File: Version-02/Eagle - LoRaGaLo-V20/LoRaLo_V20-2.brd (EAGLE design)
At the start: 69.5 x 82.5 mm, 31 parts, among them U2 RFM95WSMD

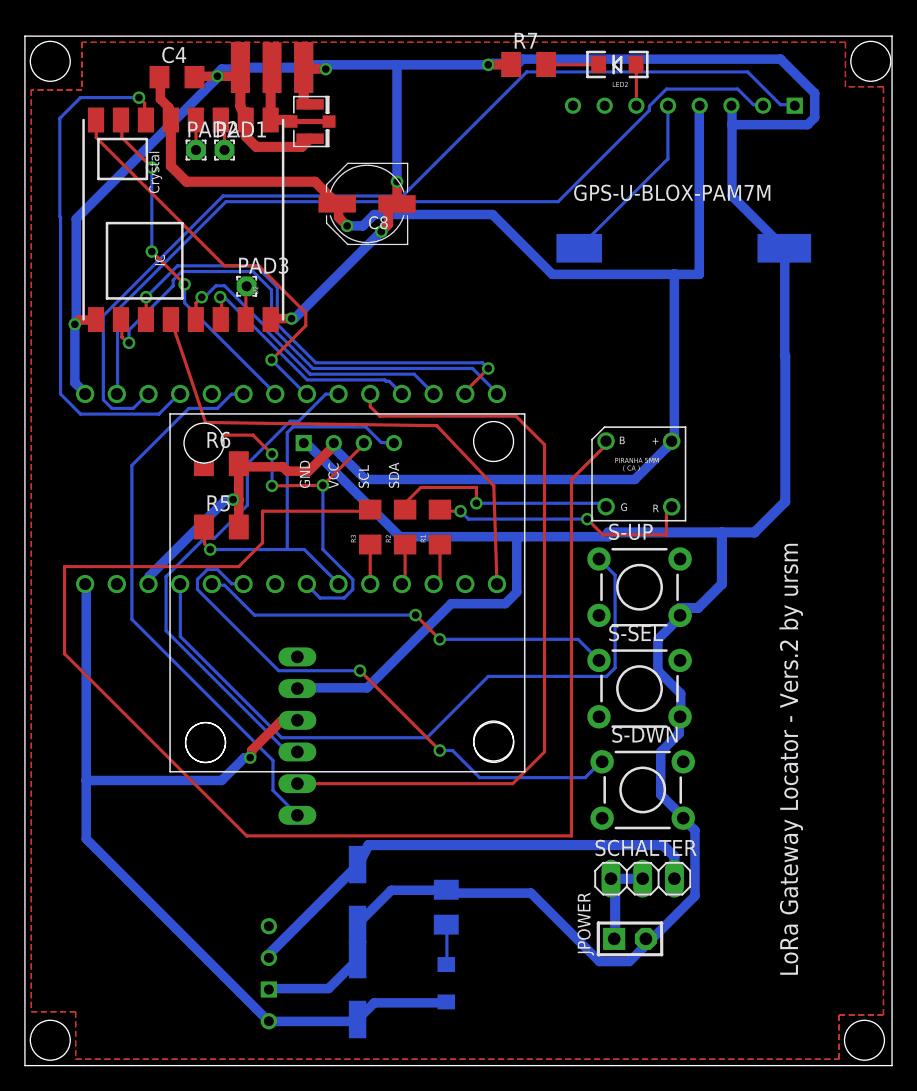
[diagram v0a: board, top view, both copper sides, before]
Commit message: V20-2 Rerouted
a better routed board
also 4 holes for the OLED
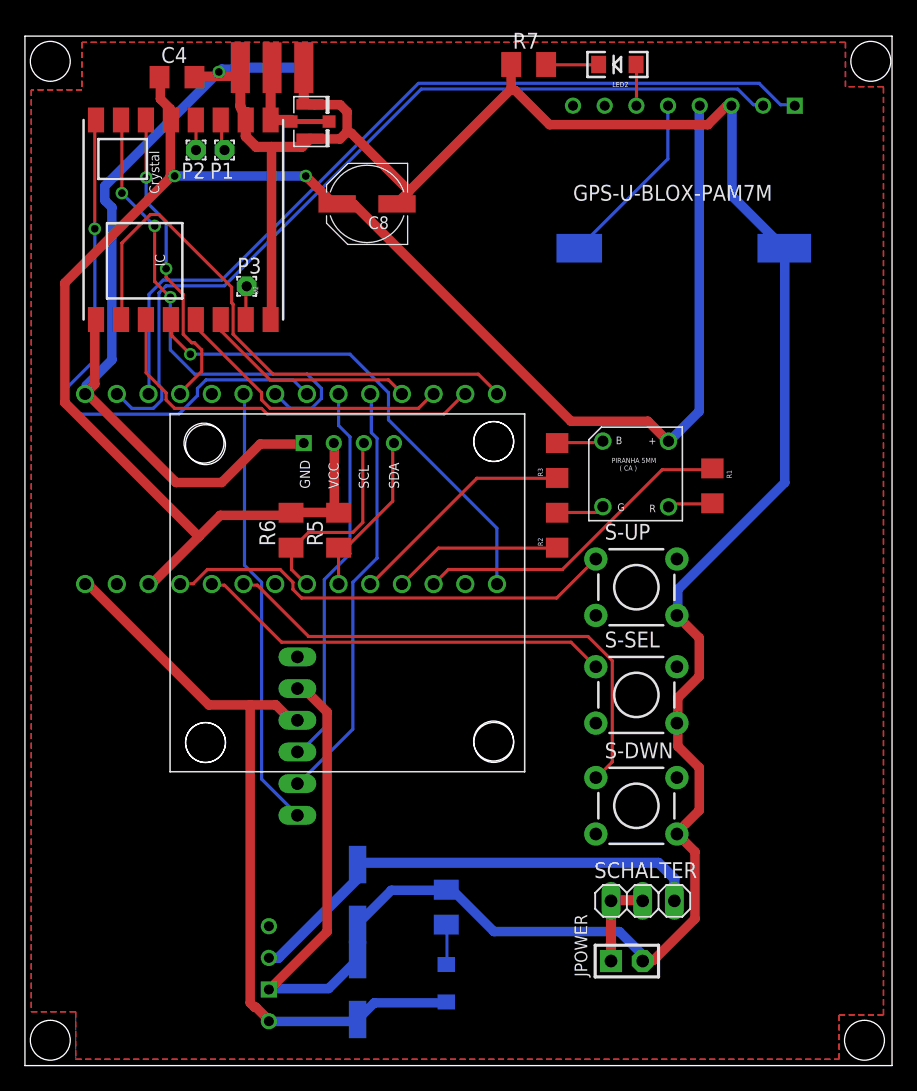
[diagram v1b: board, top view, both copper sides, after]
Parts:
- removed RGBLED: LED_PIRANHA_5MM, SparkFun-LED_mod:LED_PIRANHA_5MM
- added RGB-LED: LED_PIRANHA_5MM, SparkFun-LED_mod:LED_PIRANHA_5MM
- OLED_128X64: value OLED_128X64 -> (none)
- TEENSY-3.2: value TEENSY_3.1_DIL -> (none)
- moved R1 22.1 mm to (55.1, 46.5), turned to 270 degrees
- moved R3 15.9 mm to (42.7, 48.5)
- moved R2 12.2 mm to (42.7, 42.9)
- moved R5 9.40 mm to (25.1, 42.9), turned to 90 degrees
- moved R6 7.73 mm to (21.3, 42.9), turned to 90 degrees
- moved JPOWER 1.80 mm to (48.3, 8.38)
- moved SCHALTER 1.78 mm to (49.5, 13.2)
- moved S-DWN 1.37 mm to (49.0, 20.8)
- moved S-SEL 0.57 mm to (49.0, 29.7)
- moved S-UP 0.25 mm to (49.0, 38.4)
- turned P1 to 180 degrees
- turned P2 to 180 degrees
- renumbered PAD1 to P1, PAD2 to P2, PAD3 to P3, U$2 to OLED_128X64
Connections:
- net 3.3V: now also RGB-LED.+; no longer RGBLED.+
- net N$1: now also RGB-LED.R; no longer RGBLED.R
- net N$3: now also RGB-LED.G; no longer RGBLED.G
- net N$9: now also RGB-LED.B; no longer RGBLED.B
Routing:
- net N$9: track 114.3 -> 3.72 mm
- net RXI: track 61.8 -> 34.2 mm
- net GND: track 320.2 -> 292.8 mm, vias 7 -> 1
- net LED-RED: track 3.38 -> 26.2 mm
- net SDA0: track 32.1 -> 13.5 mm, vias 1 -> 0
- net N$1: track 21.4 -> 3.64 mm, vias 2 -> 0
- net UP: track 54.0 -> 36.4 mm
- net DIO0: track 42.1 -> 24.7 mm, vias 1 -> 2
- net SCL0: track 33.0 -> 16.5 mm, vias 3 -> 0
- net LED-BLUE: track 3.17 -> 18.5 mm
- net N$3: track 18.5 -> 3.86 mm, vias 1 -> 0
- net VCC: track 75.2 -> 62.5 mm, vias 1 -> 0
- net DIO2: track 32.9 -> 45.1 mm
- net DIO1: track 27.1 -> 38.8 mm
- net LED-GREEN: track 3.28 -> 13.6 mm
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- added copper zone on layer 16, net N$13
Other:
- board text added: "LoRaWan Gateway Locator by ursm"
- board text removed: "LoRa Gateway Locator - Vers.2 by ursm"
